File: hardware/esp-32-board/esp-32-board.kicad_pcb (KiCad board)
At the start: 2 copper layers, 53.8 x 69.1 mm, 34 parts, among them J1 MainConnector, J2 Conn_01x06, J3 ESP-PROG-Program, J4 ESP-PROG-Debug, J5 USB_B_Micro, J6 Barrel_Jack_MountingPin, Q1 BCR129S, SW1 SW_Push, SW2 SW_Push, SW3 SW_DPDT_x2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

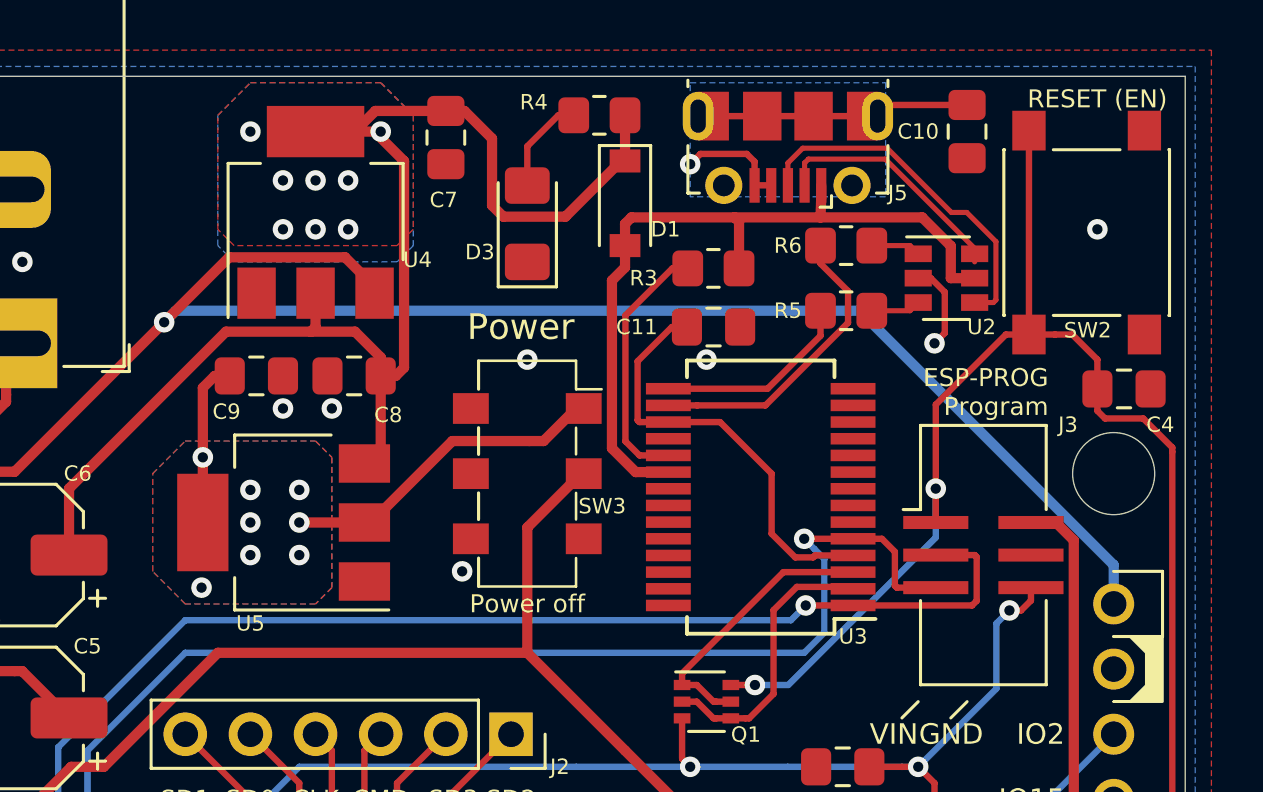
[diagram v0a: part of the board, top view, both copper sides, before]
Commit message: Expose 5V instead of VIN on main connector
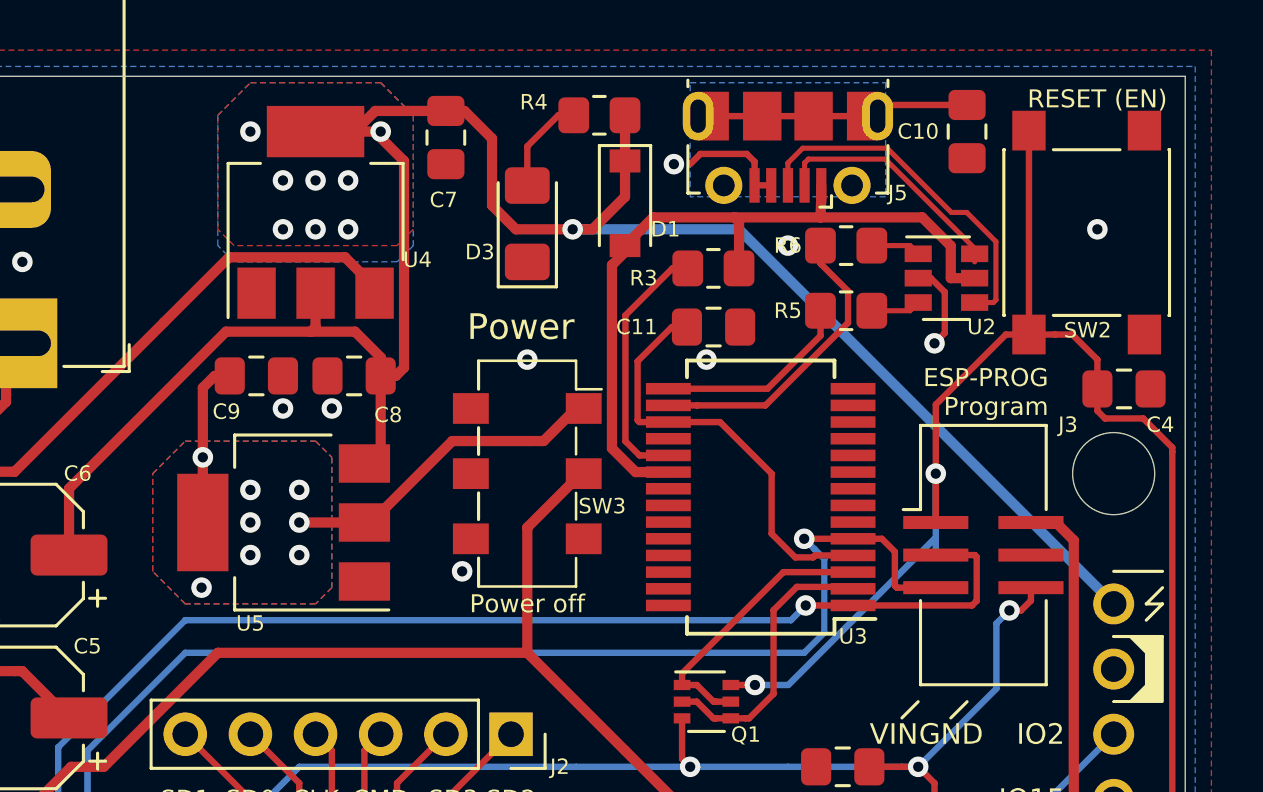
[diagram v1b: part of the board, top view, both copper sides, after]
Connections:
- J1 pad 33: VDC -> +5V
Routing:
- net VDC: track 82.4 -> 39.6 mm, vias 1 -> 0
- net +5V: track 55.4 -> 84.0 mm, vias 8 -> 9
- net /EN: track 116.5 -> 117.8 mm
- net GND: vias 15 -> 16
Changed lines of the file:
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@@
   (general
     (thickness 1.6)
-    (drawings 76)
-    (tracks 539)
+    (drawings 78)
+    (tracks 538)
     (zones 0)
     (modules 34)
@@
   (layers
     (0 F.Cu signal)
-    (31 B.Cu signal hide)
+    (31 B.Cu signal)
     (32 B.Adhes user hide)
     (33 F.Adhes user hide)
@@
     (add_net "Net-(C11-Pad1)")
     (add_net "Net-(D3-Pad2)")
-    (add_net "Net-(J4-Pad10)")
     (add_net "Net-(J4-Pad2)")
     (add_net "Net-(J4-Pad4)")
@@
     (add_net "Net-(R5-Pad1)")
     (add_net "Net-(R6-Pad1)")
-    (add_net "Net-(SW3-Pad3)")
-    (add_net "Net-(U1-Pad32)")
-    (add_net "Net-(U3-Pad10)")
-    (add_net "Net-(U3-Pad11)")
-    (add_net "Net-(U3-Pad12)")
-    (add_net "Net-(U3-Pad13)")
-    (add_net "Net-(U3-Pad14)")
-    (add_net "Net-(U3-Pad22)")
-    (add_net "Net-(U3-Pad23)")
-    (add_net "Net-(U3-Pad27)")
-    (add_net "Net-(U3-Pad28)")
-    (add_net "Net-(U3-Pad6)")
-    (add_net "Net-(U3-Pad9)")
   )
   (net_class Power ""
@@
       (net 3 +3V3))
     (pad 33 thru_hole oval (at -7.62 -48.26 180) (size 1.6 1.6) (drill 1) (layers *.Cu *.Mask)
-      (net 41 VDC))
+      (net 2 +5V))
     (pad 30 thru_hole oval (at 0 -48.26 180) (size 1.6 1.6) (drill 1) (layers *.Cu *.Mask)
       (net 24 /IO15))
@@
     )
   )
+  (gr_line (start 182.245 41.91) (end 181.61 42.545) (layer F.SilkS) (width 0.12))
+  (gr_line (start 181.61 41.91) (end 182.245 41.91) (layer F.SilkS) (width 0.12))
+  (gr_line (start 182.245 41.275) (end 181.61 41.91) (layer F.SilkS) (width 0.12))
   (gr_line (start 130.175 48.26) (end 132.08 48.26) (layer F.SilkS) (width 0.12))
   (gr_line (start 132.08 50.8) (end 130.175 50.8) (layer F.SilkS) (width 0.12))
@@
   (gr_line (start 182.245 43.18) (end 180.34 43.18) (layer F.SilkS) (width 0.12))
   (gr_line (start 180.34 40.64) (end 182.245 40.64) (layer F.SilkS) (width 0.12))
-  (gr_line (start 182.245 40.64) (end 182.245 43.18) (layer F.SilkS) (width 0.12))
   (gr_line (start 182.245 86.36) (end 180.34 86.36) (layer F.SilkS) (width 0.12))
   (gr_line (start 182.245 83.82) (end 182.245 86.36) (layer F.SilkS) (width 0.12))
@@
   (via (at 152.4 86.36) (size 0.8) (drill 0.4) (layers F.Cu B.Cu) (net 1))
   (via (at 136.525 42.545) (size 0.8) (drill 0.4) (layers F.Cu B.Cu) (net 1))
-  (via (at 163.83 24.765) (size 0.8) (drill 0.4) (layers F.Cu B.Cu) (net 1))
   (via (at 173.355 31.75) (size 0.8) (drill 0.4) (layers F.Cu B.Cu) (net 1))
   (via (at 179.705 27.305) (size 0.8) (drill 0.4) (layers F.Cu B.Cu) (net 1))
@@
   (segment (start 173.754999 29.754997) (end 173.754999 31.350001) (width 0.25) (layer F.Cu) (net 1))
   (segment (start 173.210002 29.21) (end 173.754999 29.754997) (width 0.25) (layer F.Cu) (net 1))
+  (via (at 167.64 27.94) (size 0.8) (drill 0.4) (layers F.Cu B.Cu) (net 1))
+  (via (at 163.195 24.765) (size 0.8) (drill 0.4) (layers F.Cu B.Cu) (net 1))
   (segment (start 161.29 24.64) (end 161.29 22.86) (width 0.4) (layer F.Cu) (net 2))
   (segment (start 151.765 32.585) (end 151.765 33.02) (width 0.4) (layer F.Cu) (net 2))
-  (segment (start 156.544332 26.81251) (end 158.96749 26.81251) (width 0.4) (layer F.Cu) (net 2))
-  (segment (start 156.10499 26.373168) (end 156.544332 26.81251) (width 0.4) (layer F.Cu) (net 2))
   (segment (start 156.10499 23.76499) (end 156.10499 26.373168) (width 0.4) (layer F.Cu) (net 2))
   (segment (start 161.14 24.64) (end 161.29 24.64) (width 0.4) (layer F.Cu) (net 2))
   (segment (start 155.03 22.69) (end 156.10499 23.76499) (width 0.4) (layer F.Cu) (net 2))
-  (segment (start 158.96749 26.81251) (end 161.14 24.64) (width 0.4) (layer F.Cu) (net 2))
   (segment (start 154.305 22.69) (end 155.03 22.69) (width 0.4) (layer F.Cu) (net 2))
   (segment (start 149.225 23.495) (end 150.749 23.495) (width 0.4) (layer F.Cu) (net 2))
@@
   (segment (start 160.655 67.31) (end 164.465 67.31) (width 0.25) (layer B.Cu) (net 5))
   (segment (start 177.038 23.457) (end 177.038 31.407) (width 0.25) (layer F.Cu) (net 5))
-  (segment (start 176.138 31.407) (end 177.038 31.407) (width 0.25) (layer F.Cu) (net 5))
-  (segment (start 173.405 34.14) (end 176.138 31.407) (width 0.25) (layer F.Cu) (net 5))
-  (segment (start 173.405 38.735) (end 173.405 37.415) (width 0.25) (layer F.Cu) (net 5))
   (segment (start 178.054 31.407) (end 177.038 31.407) (width 0.25) (layer F.Cu) (net 5))
   (segment (start 180.34 82.55) (end 182.626 80.264) (width 0.25) (layer F.Cu) (net 5))
@@
   (segment (start 166.355 45.07) (end 166.355 45.07) (width 0.25) (layer F.Cu) (net 5))
   (via (at 166.355 45.07) (size 0.8) (drill 0.4) (layers F.Cu B.Cu) (net 5))
-  (segment (start 173.405 37.415) (end 173.405 34.14) (width 0.25) (layer F.Cu) (net 5))
-  (via (at 173.405 37.415) (size 0.8) (drill 0.4) (layers F.Cu B.Cu) (net 5))
-  (segment (start 173.405 37.980685) (end 173.405 37.415) (width 0.25) (layer B.Cu) (net 5))
-  (segment (start 173.405 39.32141) (end 173.405 37.980685) (width 0.25) (layer B.Cu) (net 5))
-  (segment (start 167.65641 45.07) (end 173.405 39.32141) (width 0.25) (layer B.Cu) (net 5))
-  (segment (start 166.355 45.07) (end 167.65641 45.07) (width 0.25) (layer B.Cu) (net 5))
+  (via (at 173.405 36.83) (size 0.8) (drill 0.4) (layers F.Cu B.Cu) (net 5))
   (segment (start 151.13 47.625) (end 151.765 46.99) (width 0.25) (layer F.Cu) (net 6))
   (segment (start 151.13 52.34) (end 151.13 47.625) (width 0.25) (layer F.Cu) (net 6))
@@
   (segment (start 150.375 28.395) (end 151.525 29.545) (width 0.4) (layer F.Cu) (net 41))
   (segment (start 143.322499 30.927499) (end 145.854998 28.395) (width 0.4) (layer F.Cu) (net 41))
-  (via (at 143.322499 30.927499) (size 0.8) (drill 0.4) (layers F.Cu B.Cu) (net 41))
   (segment (start 131.572 44.616) (end 131.572 45.466) (width 0.4) (layer F.Cu) (net 41))
   (segment (start 132.872 43.316) (end 131.572 44.616) (width 0.4) (layer F.Cu) (net 41))
@@
   (segment (start 135.743736 36.756008) (end 132.872001 39.627743) (width 0.4) (layer F.Cu) (net 41))
   (segment (start 137.49399 36.756008) (end 135.743736 36.756008) (width 0.4) (layer F.Cu) (net 41))
-  (segment (start 170.43 30.48) (end 180.34 40.39) (width 0.4) (layer B.Cu) (net 41))
-  (segment (start 143.322499 30.927499) (end 143.769998 30.48) (width 0.4) (layer B.Cu) (net 41))
-  (segment (start 180.34 40.39) (end 180.34 41.91) (width 0.4) (layer B.Cu) (net 41))
-  (segment (start 143.769998 30.48) (end 170.43 30.48) (width 0.4) (layer B.Cu) (net 41))
+  (via (at 159.2475 27.305) (size 0.8) (drill 0.4) (layers F.Cu B.Cu) (net 2))
+  (segment (start 157.036822 27.305) (end 159.2475 27.305) (width 0.4) (layer F.Cu) (net 2))
+  (segment (start 156.10499 26.373168) (end 157.036822 27.305) (width 0.4) (layer F.Cu) (net 2))
+  (segment (start 161.29 24.64) (end 161.29 26.035) (width 0.4) (layer F.Cu) (net 2))
+  (segment (start 160.02 27.305) (end 159.2475 27.305) (width 0.4) (layer F.Cu) (net 2))
+  (segment (start 161.29 26.035) (end 160.02 27.305) (width 0.4) (layer F.Cu) (net 2))
+  (segment (start 165.735 27.305) (end 180.34 41.91) (width 0.4) (layer B.Cu) (net 2))
+  (segment (start 159.2475 27.305) (end 165.735 27.305) (width 0.4) (layer B.Cu) (net 2))
+  (segment (start 176.138 31.407) (end 177.038 31.407) (width 0.25) (layer F.Cu) (net 5))
+  (segment (start 173.405 34.14) (end 176.138 31.407) (width 0.25) (layer F.Cu) (net 5))
+  (segment (start 173.405 38.735) (end 173.405 34.14) (width 0.25) (layer F.Cu) (net 5))
+  (segment (start 173.405 39.95641) (end 173.405 36.83) (width 0.25) (layer B.Cu) (net 5))
+  (segment (start 166.355 45.07) (end 167.65641 45.07) (width 0.25) (layer B.Cu) (net 5))
+  (segment (start 167.65641 45.07) (end 173.405 39.32141) (width 0.25) (layer B.Cu) (net 5))
   (via (at 144.83 36.195) (size 0.8) (drill 0.4) (layers F.Cu B.Cu) (net 42))
   (via (at 144.78 41.275) (size 0.8) (drill 0.4) (layers F.Cu B.Cu) (net 42))
@@
   (segment (start 173.989996 27.954994) (end 173.99 29.21) (width 0.4) (layer F.Cu) (net 48))
   (segment (start 168.91 26.83999) (end 172.874992 26.83999) (width 0.4) (layer F.Cu) (net 48))
-  (segment (start 161.29 27.09) (end 161.29 27.94) (width 0.4) (layer F.Cu) (net 48))
-  (segment (start 161.54001 26.83999) (end 161.29 27.09) (width 0.4) (layer F.Cu) (net 48))
   (segment (start 165.56501 26.83999) (end 165.735 27.00998) (width 0.4) (layer F.Cu) (net 48))
   (segment (start 165.735 27.00998) (end 165.735 28.829) (width 0.4) (layer F.Cu) (net 48))
-  (segment (start 165.56501 26.83999) (end 161.54001 26.83999) (width 0.4) (layer F.Cu) (net 48))
   (segment (start 168.91 26.83999) (end 165.56501 26.83999) (width 0.4) (layer F.Cu) (net 48))
-  (segment (start 161.29 28.79) (end 160.780001 29.299999) (width 0.4) (layer F.Cu) (net 48))
-  (segment (start 161.29 27.94) (end 161.29 28.79) (width 0.4) (layer F.Cu) (net 48))
-  (segment (start 161.705 36.77) (end 162.98 36.77) (width 0.4) (layer F.Cu) (net 48))
-  (segment (start 160.780001 35.845001) (end 161.705 36.77) (width 0.4) (layer F.Cu) (net 48))
-  (segment (start 160.780001 29.299999) (end 160.780001 35.845001) (width 0.4) (layer F.Cu) (net 48))
+  (segment (start 161.925 27.305) (end 161.29 27.94) (width 0.4) (layer F.Cu) (net 48))
+  (segment (start 165.56501 26.83999) (end 162.39001 26.83999) (width 0.4) (layer F.Cu) (net 48))
+  (segment (start 162.39001 26.83999) (end 161.925 27.305) (width 0.4) (layer F.Cu) (net 48))
+  (segment (start 161.29 28.190002) (end 161.29 27.94) (width 0.4) (layer F.Cu) (net 48))
+  (segment (start 160.780001 28.700001) (end 161.29 28.190002) (width 0.4) (layer F.Cu) (net 48))
+  (segment (start 162.98 36.77) (end 161.705 36.77) (width 0.4) (layer F.Cu) (net 48))
+  (segment (start 160.780001 35.845001) (end 160.780001 28.700001) (width 0.4) (layer F.Cu) (net 48))
+  (segment (start 161.705 36.77) (end 160.780001 35.845001) (width 0.4) (layer F.Cu) (net 48))
   (segment (start 158.69 22.86) (end 159.29 22.86) (width 0.25) (layer F.Cu) (net 49))
   (segment (start 157.48 24.07) (end 158.69 22.86) (width 0.25) (layer F.Cu) (net 49))
